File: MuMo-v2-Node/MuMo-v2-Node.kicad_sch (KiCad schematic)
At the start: 76 parts, among them Q1 Si1308EDL, SW1 Boot0, SW2 Reset, U1 MCP73123, U2 LoRa-E5, U3 CP2102N, U4 eInk_Display_1.54"200x200px, U5 BME680, U6 TSL25911, U7 BR24G512FVT-5AE2

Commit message: cleaned datasheets
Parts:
- D4: footprint SOT143 -> thisProjectLibrary:SP0503BAHTG-SOT143
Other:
- moved on the sheet: CONN7, CONN8

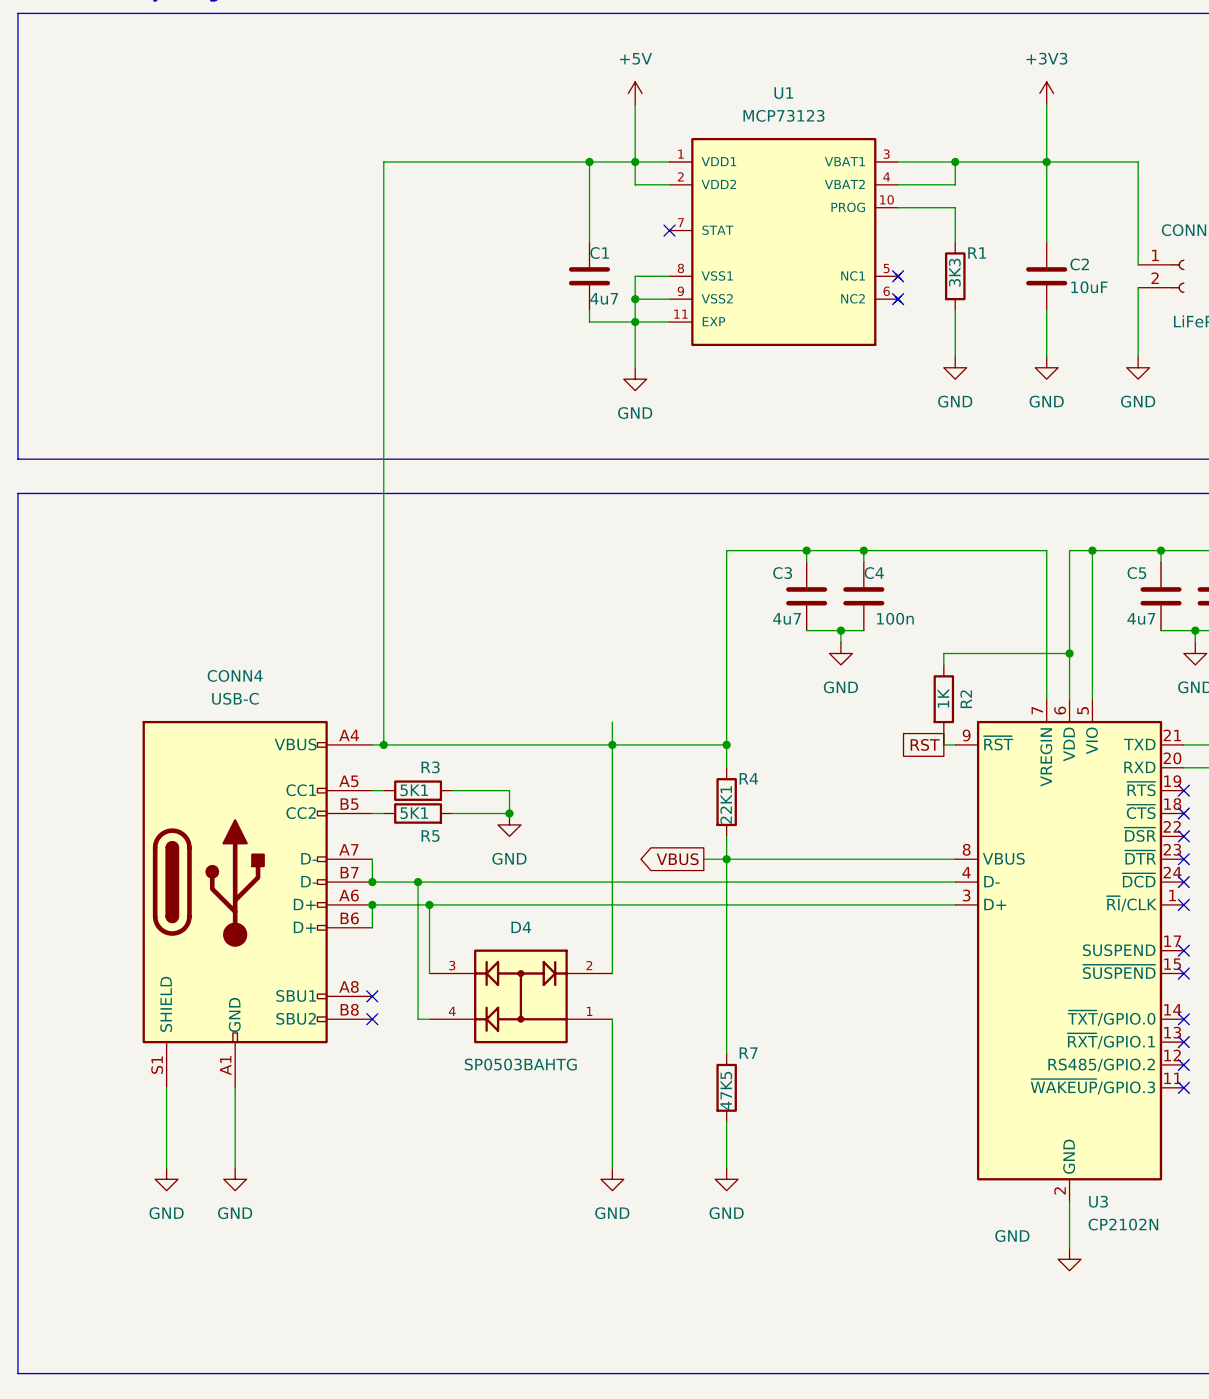
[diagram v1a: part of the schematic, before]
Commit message: fixed #1
Replaced GCT4085 connector with Molex 2171790001
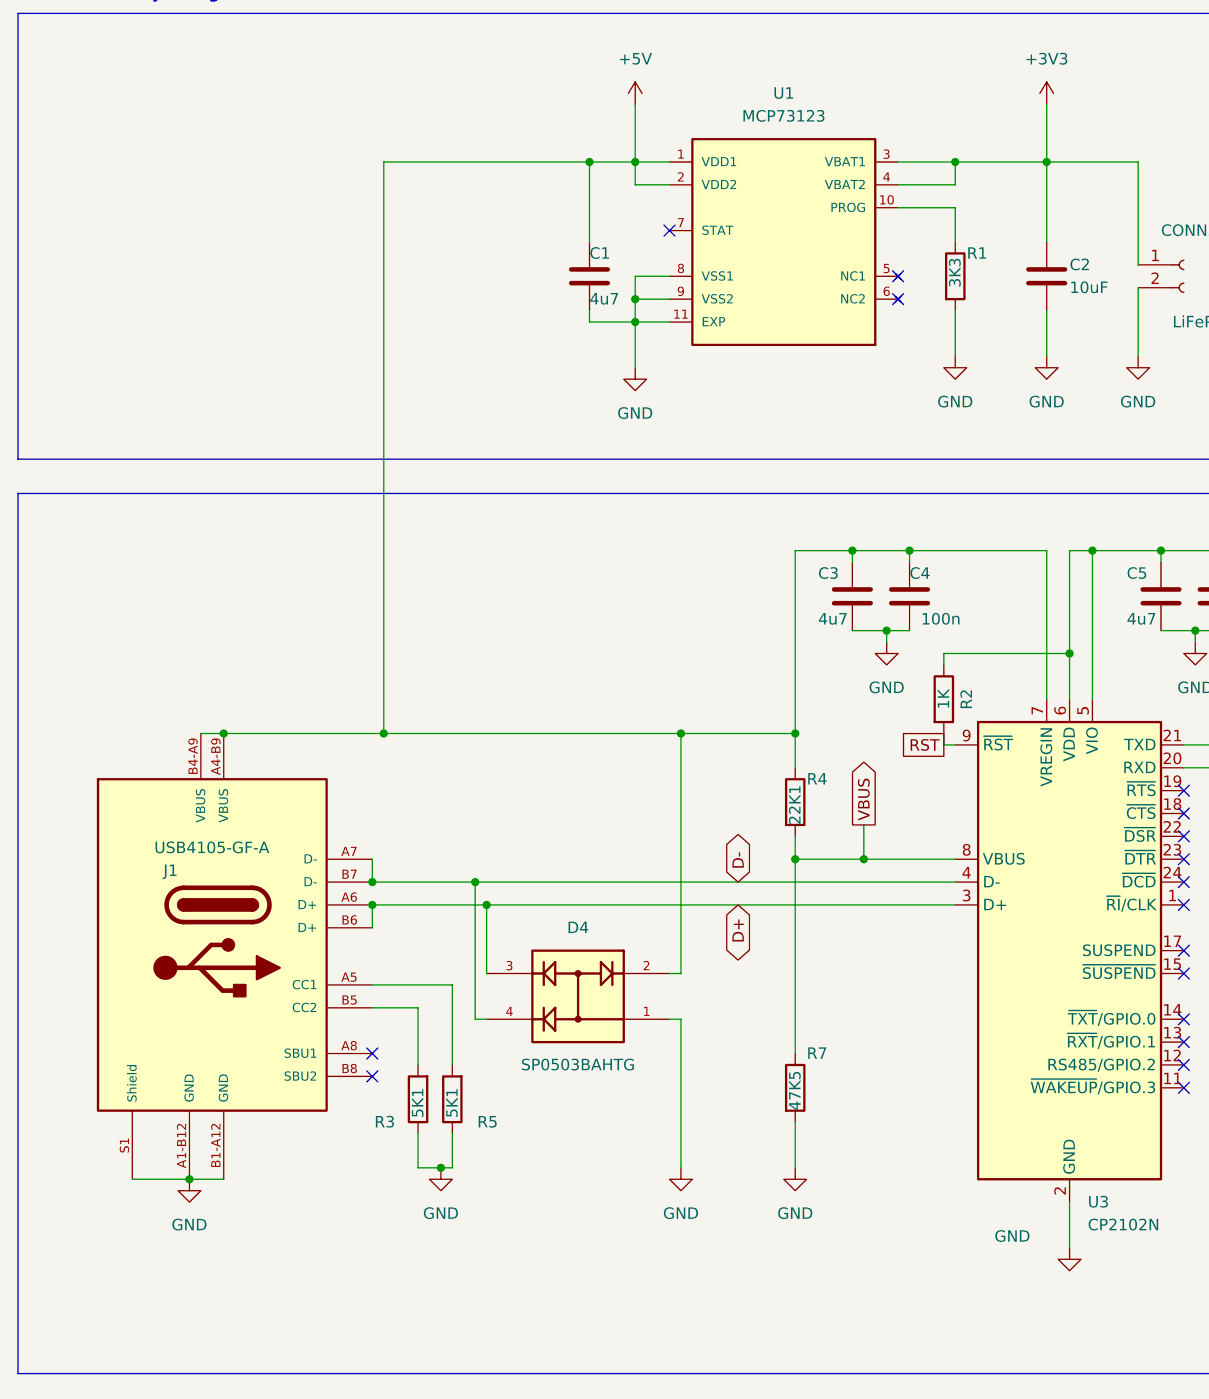
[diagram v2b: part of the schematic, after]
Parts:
- removed CONN4: USB-C, thisProjectLibrary:USB_C_Receptacle_GCT_USB4085, symbol Connector:USB_C_Receptacle_USB2.0
- added J1: USB4105-GF-A, thisProjectLibrary:Molex-2171790001, symbol thisProjectLibrary:Molex-2171790001
- C1, C10, C11, C12, C13, C14, C15, C16, C17, C18, C19, C2, C20, C21, C22, C23, C24, C25, C26, C27, C3, C4, C5, C6, C7, C8, C9, R1, R10, R11, R12, R2, R3, R4, R5, R6, R7, R8, R9: footprint Capacitor_SMD:C_0603_1608Metric -> thisProjectLibrary:0603_1608Metric
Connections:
- net +5V: now also J1.A4-B9 (VBUS), J1.B4-A9 (VBUS)
- net GND: now also R3.1, R5.1, J1.A1-B12 (GND), J1.B1-A12 (GND), J1.S1 (Shield); no longer R3.2, R5.2
- net D+: now reaches D4.3, U3.3 (D+)
- net D+: now also J1.A6 (D+), J1.B6 (D+)
- net D-: now reaches D4.4, U3.4 (D-)
- net D-: now also J1.A7 (D-), J1.B7 (D-)
- new net: J1.A5 (CC1), R5.2
- new net: J1.B5 (CC2), R3.2
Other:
- moved on the sheet: C3, C4, D4, R3, R4, R5, R7

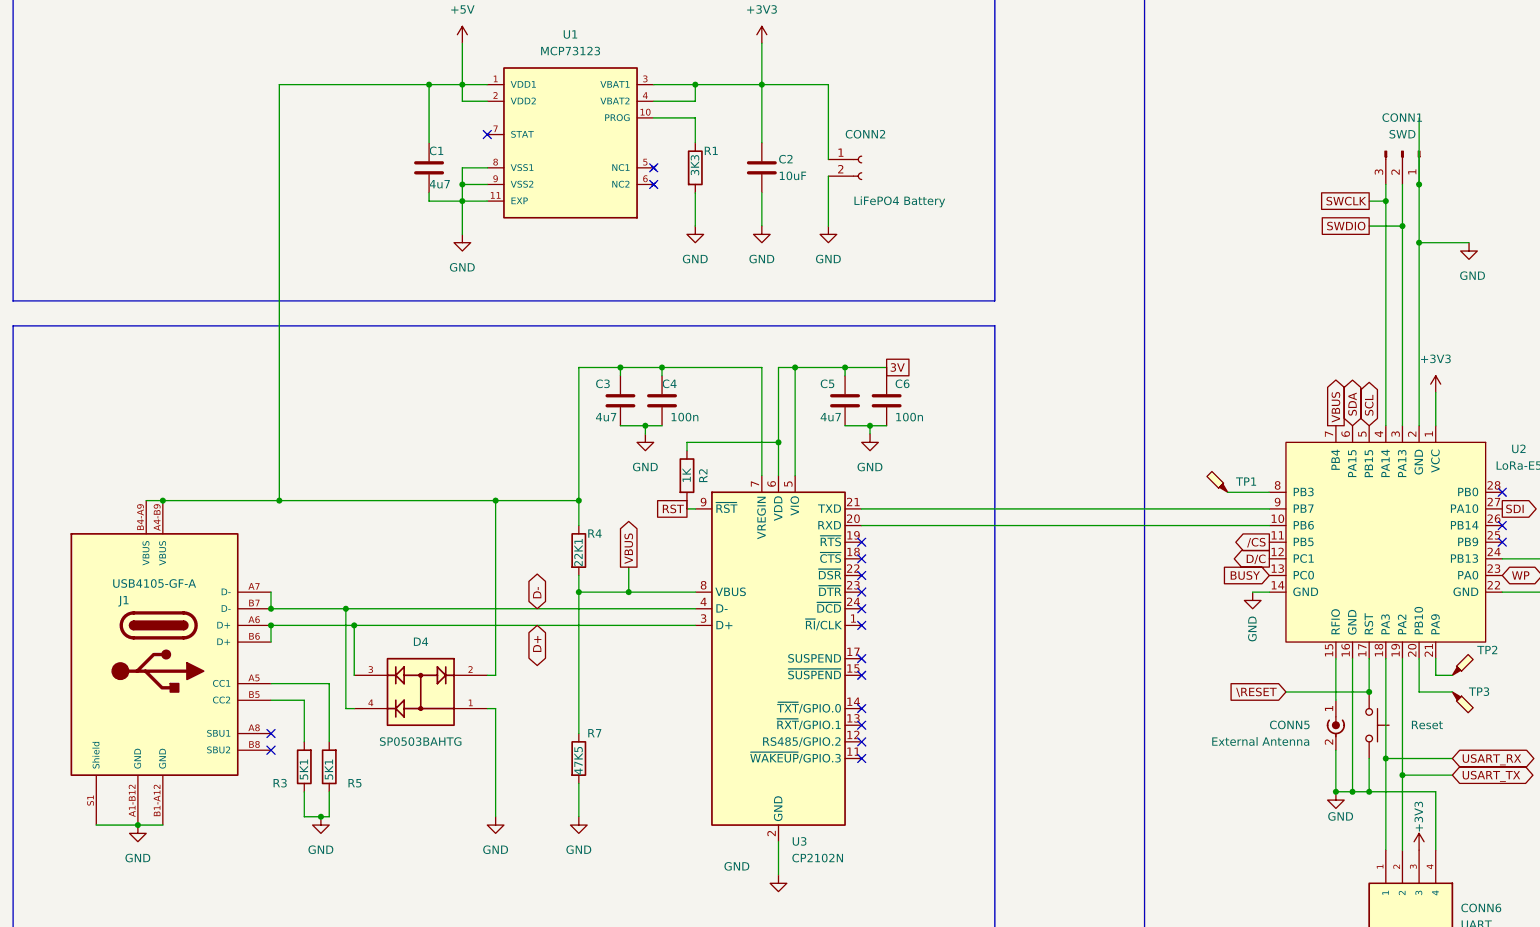
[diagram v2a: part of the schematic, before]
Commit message: Implemented improvements
#5 stitching vias
#4 USB differential pair
#6 components / values for epaper driver circuit
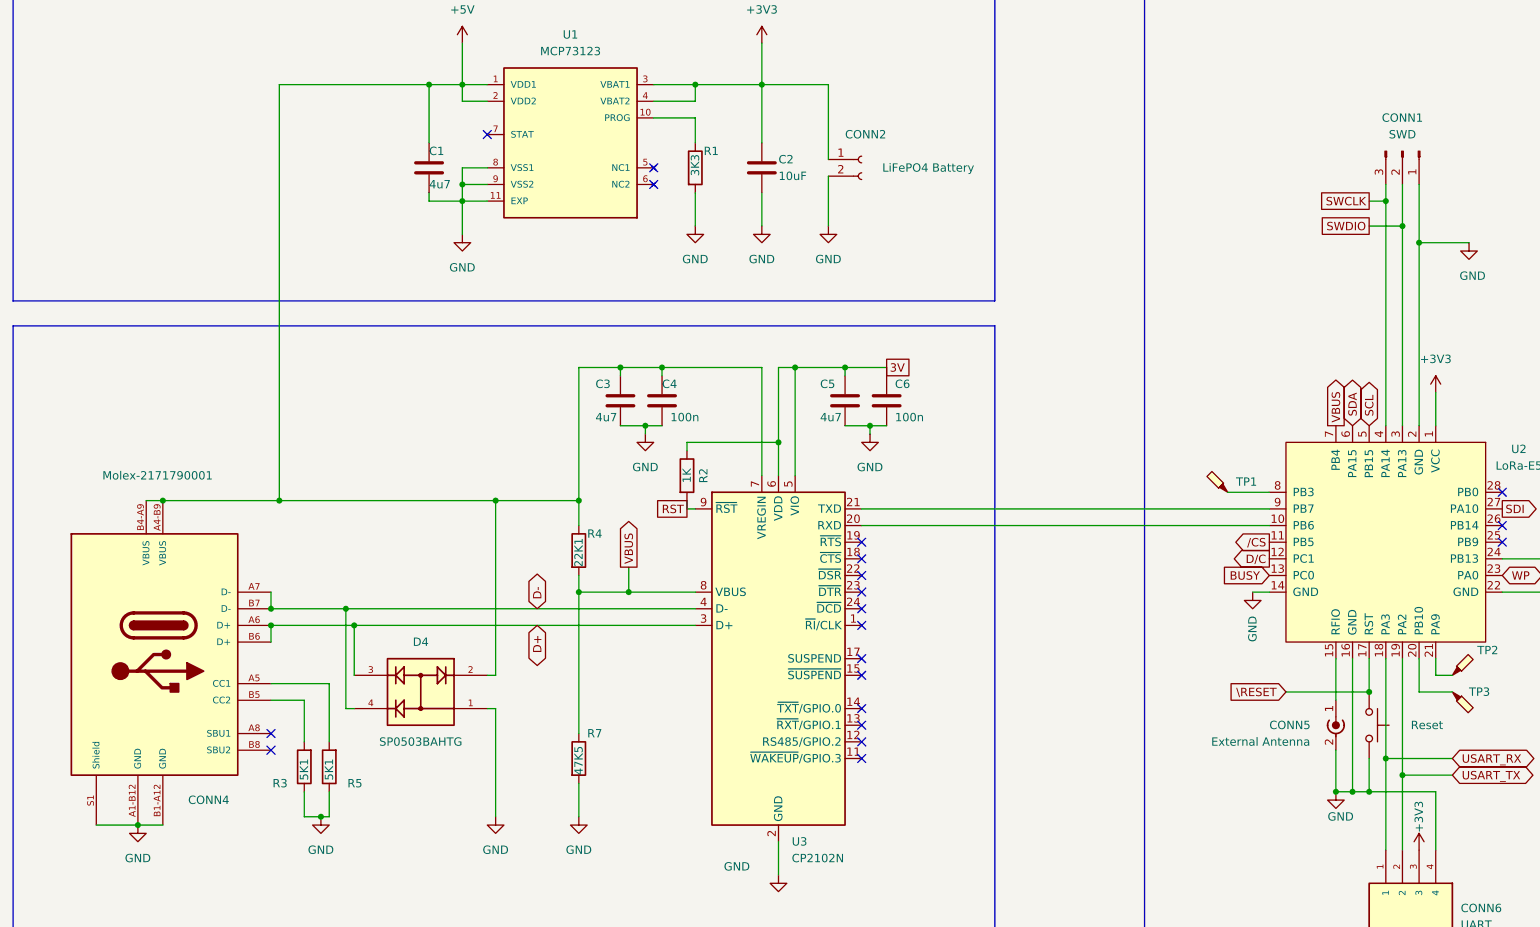
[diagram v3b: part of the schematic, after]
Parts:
- C1, C10, C11, C12, C13, C14, C15, C16, C17, C18, C19, C2, C20, C21, C22, C23, C24, C25, C26, C27, C3, C4, C5, C6, C7, C8, C9: supplier2Name (none) -> Digi-Key
- CONN1: description (none) -> 3-pin Header 2.54mm; manufacturer (none) -> Amphenol FCI; mpn notApplicable -> 10129378-903001BLF; package (none) -> 2.54mm pitch; stock (none) -> 16800; supplier1Name notApplicable -> Mouser; supplier1PartNumber (none) -> 649-1012937890301BLF; supplier1PartURL (none) -> https://www.mouser.be/ProductDetail/Amphenol-FCI/10129378-9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; supplier2Name (none) -> Digi-Key; unitPrice (none) -> 0.1
- CONN2: value LiFePO4 Battery -> B2B-XH-A (LF)(SN); description (none) -> JST XH 2pin THT Vertical; remark (none) -> LiFePO4 Battery; supplier2Name (none) -> Digi-Key; supplier2PartNumber (none) -> 455-2247-ND; supplier2PartURL (none) -> https://www.digikey.be/nl/products/detail/jst-sales-america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
- CONN3: description (none) -> FFC & FPC connectoren FPC CONN 0.5MM PITCH T/C 24P; mpn (none) -> 2-1734839-4; package (none) -> 24-pin FPC top copntact 0.5mm pitch; stock (none) -> 9000; supplier2Name (none) -> Digi-Key
- CONN4: renamed from J1; value USB4105-GF-A -> Molex-2171790001; MANUFACTURER Molex -> (none); description (none) -> USB-C receptable; manufacturer (none) -> Molex; mpn (none) -> 2171790001; package (none) -> SMT - 16-pin; stock (none) -> 18000; supplier1Name (none) -> Mouser; supplier1PartNumber (none) -> 538-217179-0001; supplier1PartURL (none) -> https://www.mouser.be/ProductDetail/Molex/217179-0001?qs=DR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; supplier2Name (none) -> Digi-Key; supplier2PartNumber (none) -> 900-2171790001CT-ND; supplier2PartURL (none) -> https://www.digikey.be/nl/products/detail/molex/2171790001/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; unitPrice (none) -> 1.19
- CONN5: description (none) -> RF-stekkers/Coaxiale stekkers SMA, Edge Mount, Female Recep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; stock (none) -> 6400; supplier2Name (none) -> Digi-Key; supplier2PartNumber (none) -> 343-CONSMA020.062-G-ND; supplier2PartURL (none) -> https://www.digikey.be/nl/products/detail/linx-technologies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
- CONN6, CONN7, CONN8: description (none) -> Grove THT Vertical PCB Male connector; stock (none) -> notApplicable; supplier2Name (none) -> Digi-Key; supplier2PartNumber (none) -> 1597-1082-ND; supplier2PartURL (none) -> https://www.digikey.be/nl/products/detail/seeed-technology-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
- D1, D2, D3: description (none) -> Schottky-diodes & gelijkrichters 1.1A .395V; mpn (none) -> SL03-GS08; package (none) -> SMF (DO-219AB); stock (none) -> 0; supplier2Name (none) -> Digi-Key; supplier2PartNumber (none) -> SL03-GS08CT-ND; supplier2PartURL (none) -> https://www.digikey.be/nl/products/detail/vishay-general-se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; unitPrice (none) -> 0.43
- D4: stock (none) -> 200000; supplier2Name (none) -> Digi-Key; supplier2PartNumber (none) -> F2715CT-ND; supplier2PartURL (none) -> https://www.digikey.be/nl/products/detail/littelfuse-inc/SP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
- F1, F2, F3, H1, H2, H3, H4: stock (none) -> notApplicable; supplier2Name (none) -> notApplicable
- L1: description (none) -> Power Inductors - SMD 68uH; mpn (none) -> VLS6045EX-680M; stock (none) -> 29000; supplier2Name (none) -> Digi-Key
- Q1: description (none) -> MOSFET 30V Vds 12V Vgs SC70-3; mpn (none) -> SI1308EDL-T1-GE3; stock (none) -> 0; supplier2Name (none) -> Digi-Key; supplier2PartNumber (none) -> SI1308EDL-T1-GE3CT-ND; supplier2PartURL (none) -> https://www.digikey.be/nl/products/detail/vishay-siliconix/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; unitPrice (none) -> 0.48
- R1, R10, R11, R12, R2, R3, R4, R5, R6, R7, R9: stock (none) -> notApplicable; supplier2Name (none) -> Digi-Key
- R8: description (none) -> Current Sense Resistors - SMD 0603 0.47ohm 1% Curr Sense AE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; manufacturer (none) -> Panasonic; mpn (none) -> ERJ-3RQFR47V; stock (none) -> 160000; supplier1PartNumber (none) -> 667-ERJ-3RQFR47V; supplier1PartURL (none) -> https://www.mouser.be/ProductDetail/Panasonic/ERJ-3RQFR47V?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; supplier2Name (none) -> Digi-Key; unitPrice (none) -> 0.17
- SW1, SW2: mpn (none) -> PTS815 SJM 250 SMTR LFS; stock (none) -> 38000; supplier2Name (none) -> Digi-Key
- TP1, TP2, TP3, TP4, TP5, TP6, TP7: supplier2Name (none) -> notApplicable
- U1: supplier2Name (none) -> Digi-Key; supplier2PartNumber (none) -> MCP73123-22SI/MF-ND; supplier2PartURL (none) -> https://www.digikey.be/nl/products/detail/microchip-technol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
- U2: supplier2Name (none) -> Digi-Key; supplier2PartNumber (none) -> 1597-317990687-ND; supplier2PartURL (none) -> https://www.digikey.be/nl/products/detail/seeed-technology-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
- U3: supplier2Name (none) -> Digi-Key; supplier2PartNumber (none) -> 336-5887-ND; supplier2PartURL (none) -> https://www.digikey.be/nl/products/detail/silicon-labs/CP21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
- U4: description (none) -> ePaper Display; manufacturer (none) -> GoodDisplay; mpn (none) -> GDEH0154D67; stock (none) -> ??; supplier1Name GoodDisplay -> Mouser; supplier1PartNumber GDEH0154D67 -> 932-MIKROE-3157; supplier1PartURL https://www.e-paper-display.com/products_detail/productId=4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 -> https://www.mouser.be/ProductDetail/Mikroe/MIKROE-3157?qs=q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; supplier2Name (none) -> GoodDisplay; supplier2PartNumber (none) -> GDEH0154D67; supplier2PartURL (none) -> https://www.e-paper-display.com/products_detail/productId=4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; unitPrice (none) -> 20
- U5: supplier2Name (none) -> Digi-Key; supplier2PartNumber (none) -> 828-1077-1-ND; supplier2PartURL (none) -> https://www.digikey.be/nl/products/detail/bosch-sensortec/B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
- U6: supplier2Name (none) -> Digi-Key; supplier2PartNumber (none) -> TSL25911FNCT-ND; supplier2PartURL (none) -> https://www.digikey.be/nl/products/detail/ams-osram/TSL2591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
- U7: supplier2Name (none) -> Digi-Key; supplier2PartNumber (none) -> 846-BR24G512FVT-5AE2CT-ND; supplier2PartURL (none) -> https://www.digikey.be/nl/products/detail/rohm-semiconducto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
